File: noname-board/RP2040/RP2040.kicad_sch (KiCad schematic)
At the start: 0 parts

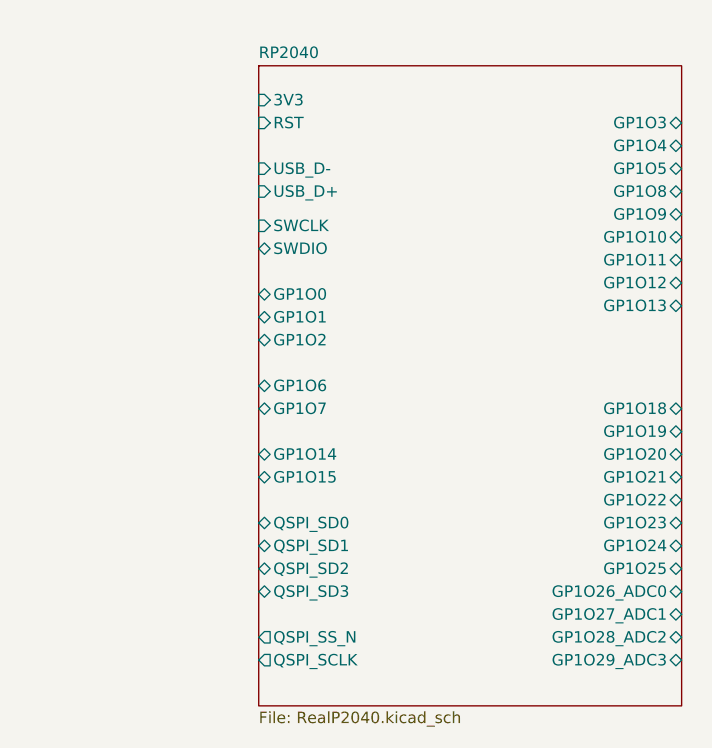
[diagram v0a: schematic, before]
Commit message: RP2040 +Flash Drive
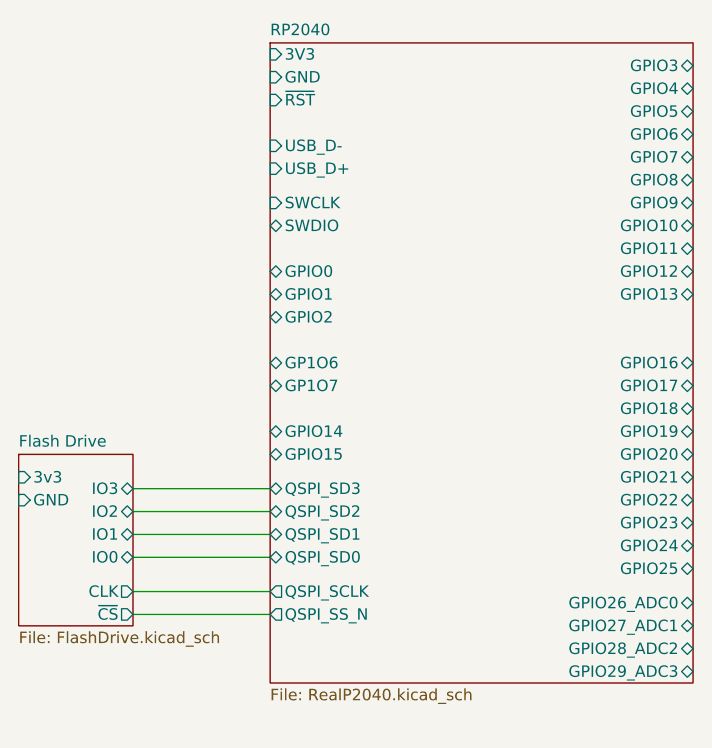
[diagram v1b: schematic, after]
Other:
- added sheet Flash Drive (FlashDrive.kicad_sch)
- sheet RP2040 ports: added GND, GPIO0, GPIO1, GPIO10, GPIO11, GPIO12, GPIO13, GPIO14, GPIO15, GPIO16, GPIO17, GPIO18, GPIO19, GPIO2, GPIO20, GPIO21, GPIO22, GPIO23, GPIO24, GPIO25, GPIO26_ADC0, GPIO27_ADC1, GPIO28_ADC2, GPIO29_ADC3, GPIO3, GPIO4, GPIO5, GPIO6, GPIO7, GPIO8, GPIO9, ~{RST}; removed GP1O0, GP1O1, GP1O10, GP1O11, GP1O12, GP1O13, GP1O14, GP1O15, GP1O18, GP1O19, GP1O2, GP1O20, GP1O21, GP1O22, GP1O23, GP1O24, GP1O25, GP1O26_ADC0, GP1O27_ADC1, GP1O28_ADC2, GP1O29_ADC3, GP1O3, GP1O4, GP1O5, GP1O8, GP1O9, RST
